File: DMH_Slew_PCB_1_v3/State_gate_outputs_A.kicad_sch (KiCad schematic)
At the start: 26 parts, among them J4 TS_Jack_6.35mm_Sw, J5 TS_Jack_6.35mm_Sw, J51 Conn_01x08_PinHeader, Q5 BC548, Q6 BC548, U1 TL074

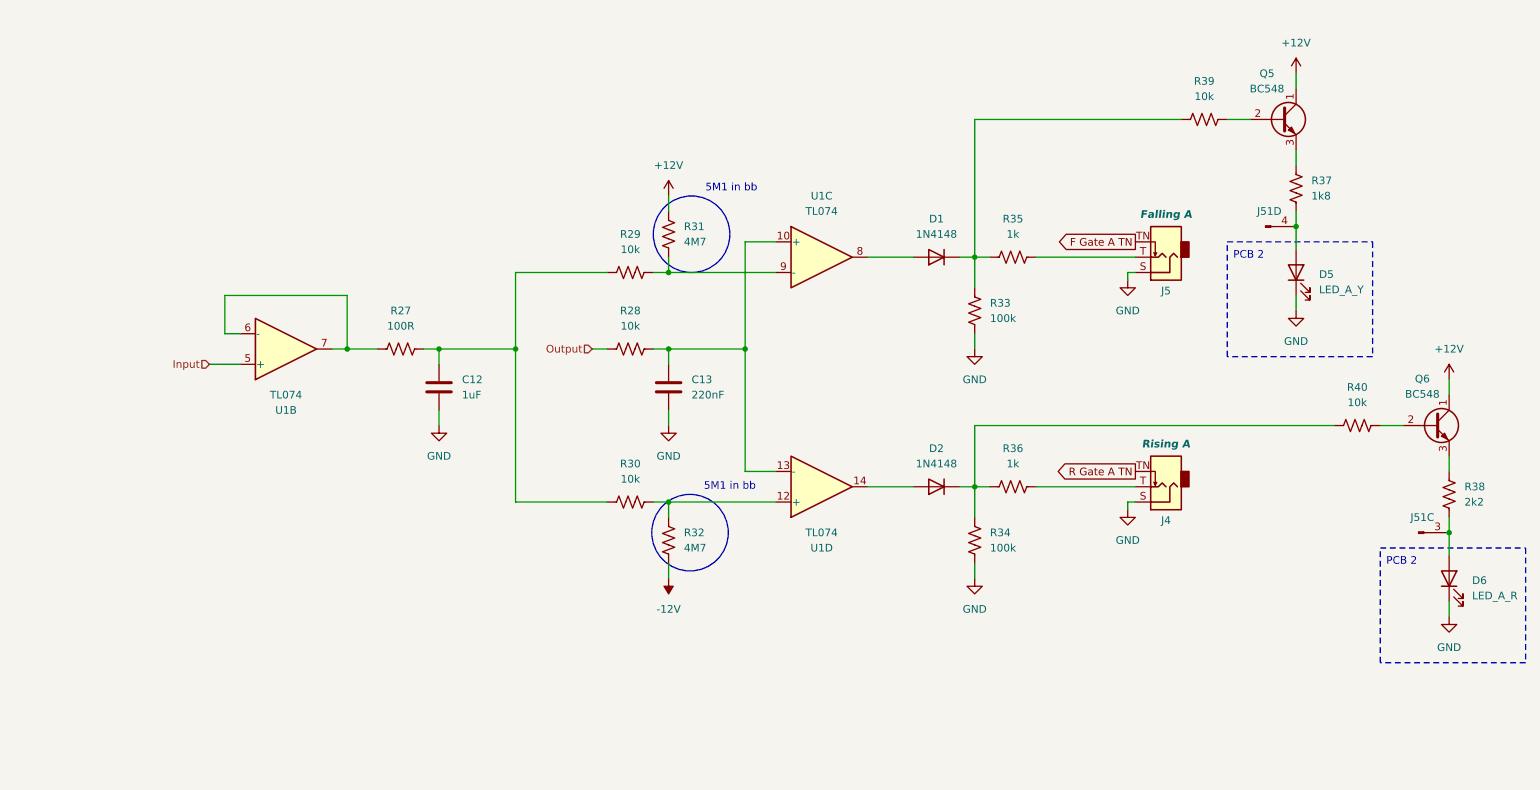
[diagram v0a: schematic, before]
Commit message: V3 sch redesign ongoing
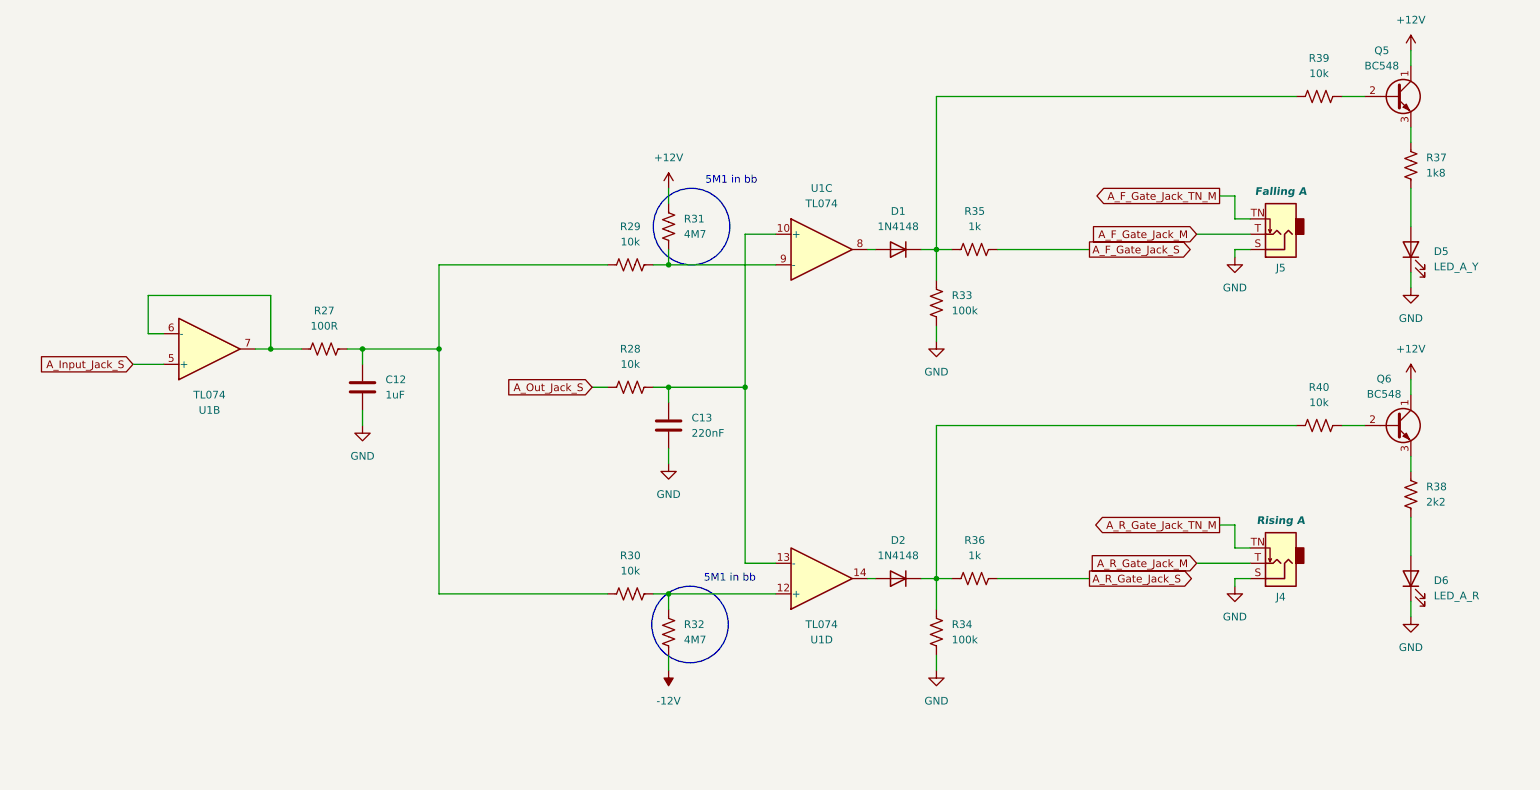
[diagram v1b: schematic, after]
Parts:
- removed J51: Conn_01x08_PinHeader, Connector_PinHeader_2.54mm:PinHeader_1x08_P2.54mm_Vertical, symbol SynthStuff:Conn_01x08_PinHeader
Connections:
- net A_F_Gate_Jack_M: now reaches J5.T
- net A_F_Gate_Jack_M: no longer R35.1
- net A_R_Gate_Jack_M: now reaches J4.T
- net A_R_Gate_Jack_M: no longer R36.1
- net F Gate A TN renamed A_F_Gate_Jack_TN_M
- net Input renamed A_Input_Jack_S
- net Output renamed A_Out_Jack_S
- net R Gate A TN renamed A_R_Gate_Jack_TN_M
- new net A_F_Gate_Jack_S: R35.1
- new net A_R_Gate_Jack_S: R36.1
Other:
- note removed: "PCB 2"
- moved on the sheet: C12, C13, D1, D2, D5, D6, J4, J5, Q5, Q6, R27, R28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

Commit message: Finished PCB1 v3 schematic
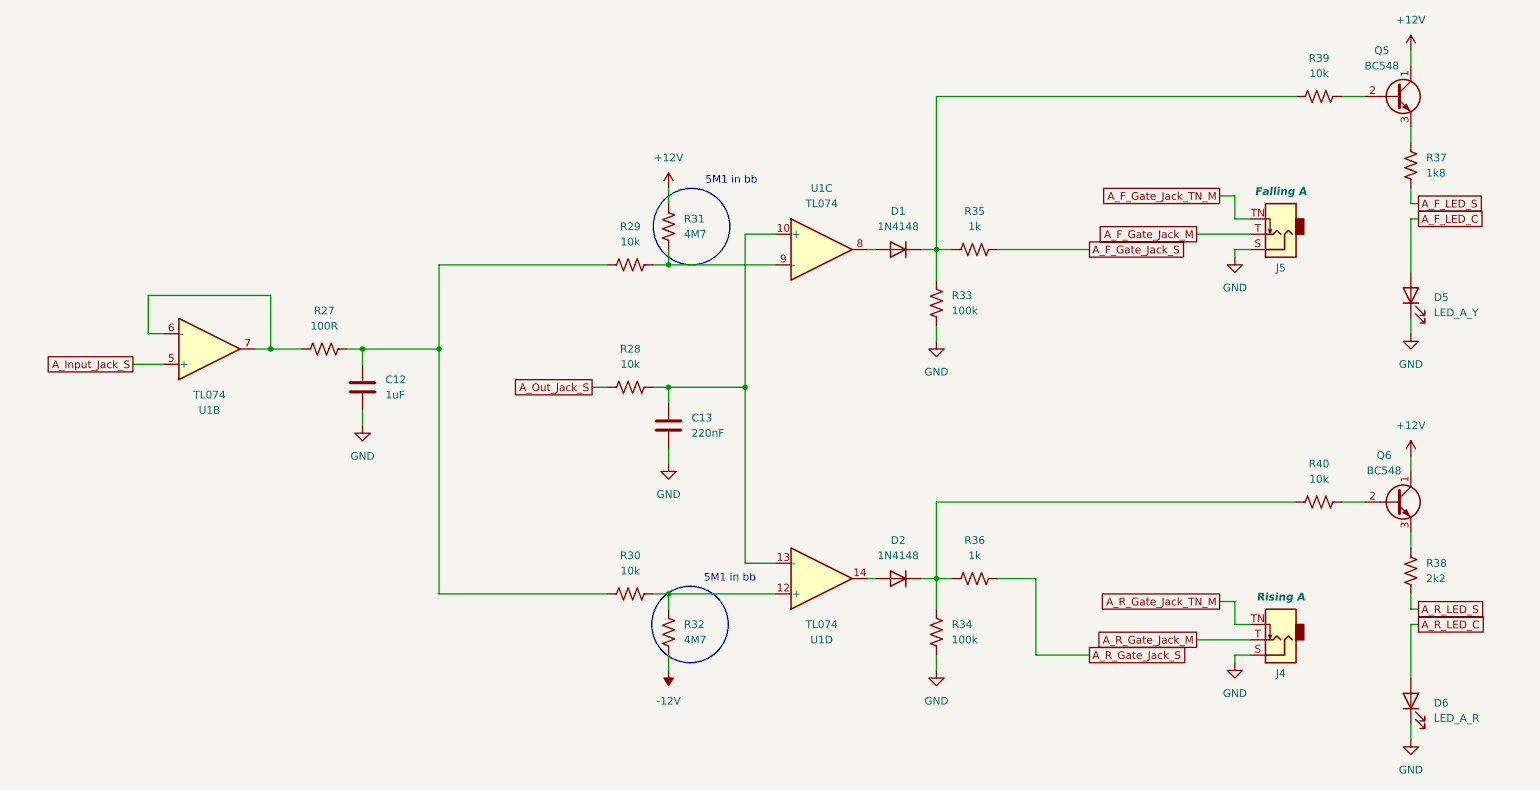
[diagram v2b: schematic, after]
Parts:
- Q5, Q6: footprint Package_TO_SOT_THT:TO-92L_Inline_Wide -> Package_TO_SOT_THT:TO-92_Inline
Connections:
- net A_R_LED_C: now reaches D6.2 (A)
- net A_R_LED_C: no longer R38.2
- net A_F_LED_C: now reaches D5.2 (A)
- net A_F_LED_C: no longer R37.2
- new net A_F_LED_S: R37.2
- new net A_R_LED_S: R38.2
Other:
- moved on the sheet: D5, D6, J4, Q6, R38, R40

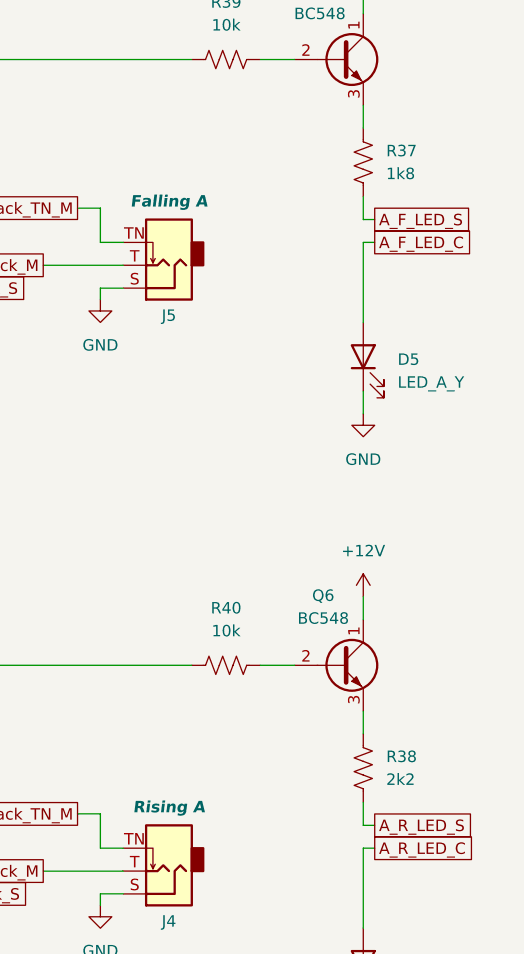
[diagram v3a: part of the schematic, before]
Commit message: Corrected PCB 2 switch positions
and Regenerated Gerbers
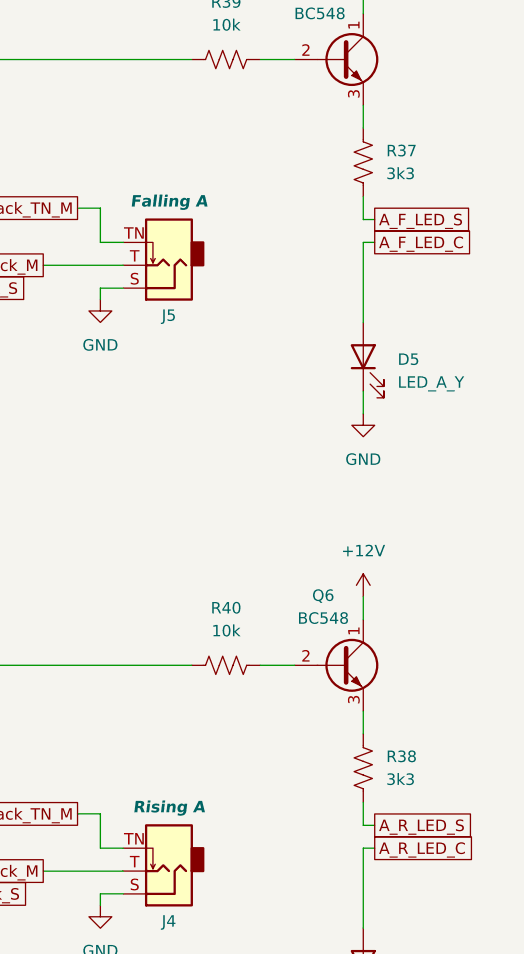
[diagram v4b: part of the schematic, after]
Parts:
- R37: value 1k8 -> 3k3
- R38: value 2k2 -> 3k3
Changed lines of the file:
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@@
 			)
 		)
-		(property "Value" "2k2"
+		(property "Value" "3k3"
 			(at 252.73 114.2999 0)
 			(effects
@@
 			)
 		)
-		(property "Value" "1k8"
+		(property "Value" "3k3"
 			(at 252.73 46.9899 0)
 			(effects

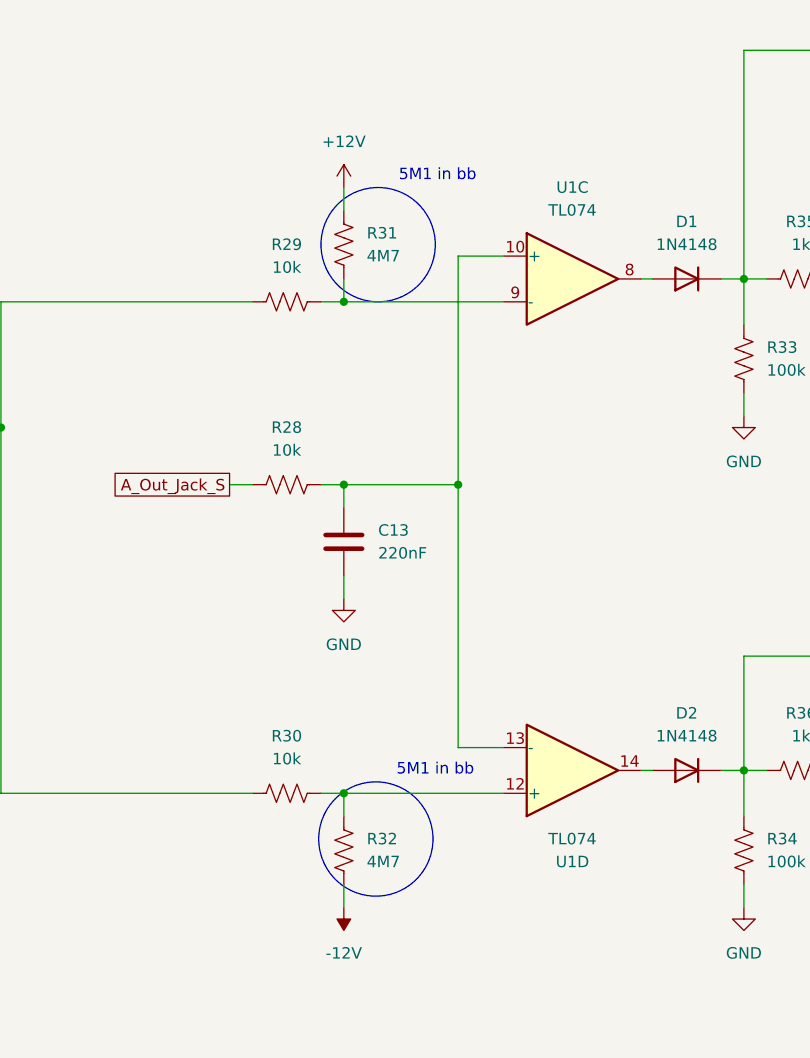
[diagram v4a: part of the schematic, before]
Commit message: Redesigned Main PCB
and regenerated Gerbers
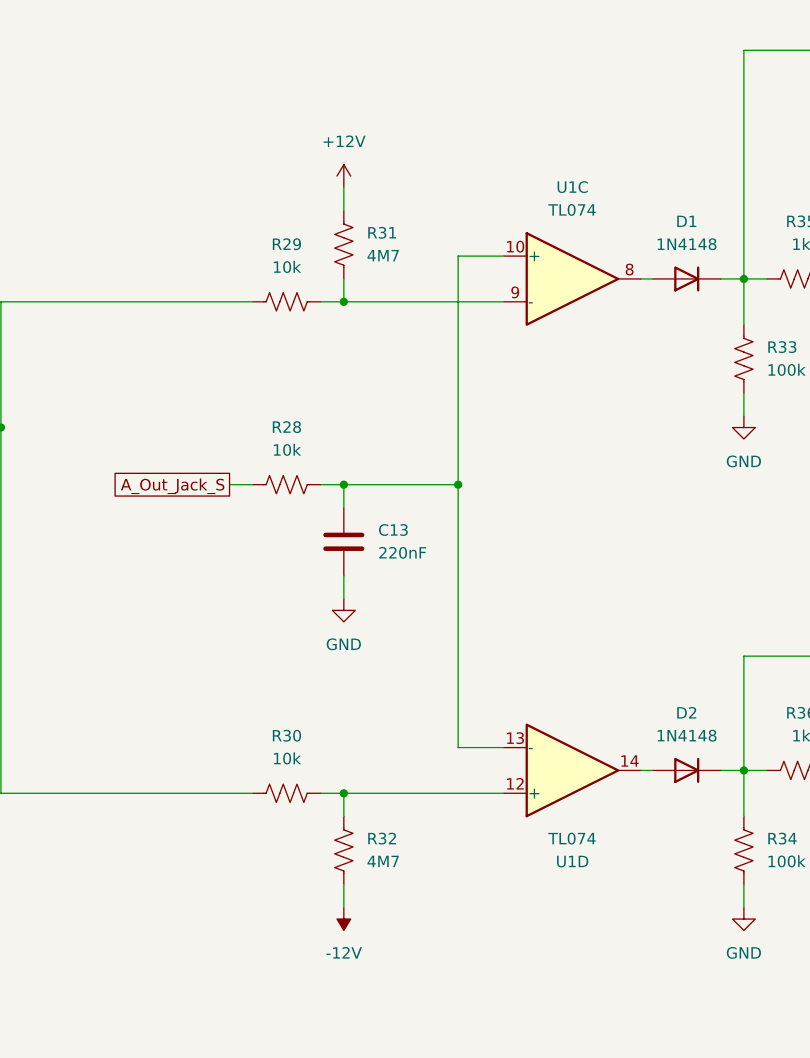
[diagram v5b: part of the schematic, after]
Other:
- note removed: "5M1 in bb"
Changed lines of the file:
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@@
 		(comment 1 "PCB for 5 cm Kosmo format synthesizer module")
-	)
-	(circle
-		(center 130.81 55.88)
-		(radius 6.35)
-		(stroke
-			(width 0)
-			(type default)
-		)
-		(fill
-			(type none)
-		)
-	)
-	(circle
-		(center 130.556 121.92)
-		(radius 6.35)
-		(stroke
-			(width 0)
-			(type default)
-		)
-		(fill
-			(type none)
-		)
-	)
-	(text "5M1 in bb"
-		(exclude_from_sim no)
-		(at 137.16 114.3 0)
-		(effects
-			(font
-				(size 1.27 1.27)
-			)
-		)
-	)
-	(text "5M1 in bb"
-		(exclude_from_sim no)
-		(at 137.414 48.26 0)
-		(effects
-			(font
-				(size 1.27 1.27)
-			)
-		)
 	)
 	(junction
